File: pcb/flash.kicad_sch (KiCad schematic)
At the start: 11 parts, among them U5 W25Q128JVS

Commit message: Add MPN field for components except resistors
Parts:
- C24: MPN (none) -> CL10B104KB8NNWC
- TP12, TP13, TP14, TP15, TP16, TP17: MPN (none) -> RCUCTE
- U5: MPN (none) -> W25Q128JVS
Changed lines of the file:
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@@
+			)
+		)
+		(property "MPN" "RCUCTE"
+			(at 63.5 73.66 0)
+			(effects
+				(font
+					(size 1.27 1.27)
+				)
+				(hide yes)
 			)
 		)
@@
 			)
 		)
+		(property "MPN" "RCUCTE"
+			(at 63.5 63.5 0)
+			(effects
+				(font
+					(size 1.27 1.27)
+				)
+				(hide yes)
+			)
+		)
 		(pin "1"
 		)
@@
 			)
 		)
+		(property "MPN" ""
+			(at 76.2 50.8 0)
+			(effects
+				(font
+					(size 1.27 1.27)
+				)
+				(hide yes)
+			)
+		)
 		(pin "2"
 		)
@@
 		)
 		(property "Description" "Resistor, small US symbol"
+			(at 88.9 50.8 0)
+			(effects
+				(font
+					(size 1.27 1.27)
+				)
+				(hide yes)
+			)
+		)
+		(property "MPN" ""
 			(at 88.9 50.8 0)
 			(effects
@@
 			)
 		)
+		(property "MPN" "W25Q128JVS"
+			(at 101.6 76.2 0)
+			(effects
+				(font
+					(size 1.27 1.27)
+				)
+				(hide yes)
+			)
+		)
 		(pin "8"
 		)
@@
 			)
 		)
+		(property "MPN" "RCUCTE"
+			(at 63.5 83.82 0)
+			(effects
+				(font
+					(size 1.27 1.27)
+				)
+				(hide yes)
+			)
+		)
 		(pin "1"
 		)
@@
 			)
 		)
+		(property "MPN" "RCUCTE"
+			(at 63.5 88.9 0)
+			(effects
+				(font
+					(size 1.27 1.27)
+				)
+				(hide yes)
+			)
+		)
 		(pin "1"
 		)
@@
 		)
 		(property "Description" "Resistor, small US symbol"
+			(at 82.55 50.8 0)
+			(effects
+				(font
+					(size 1.27 1.27)
+				)
+				(hide yes)
+			)
+		)
+		(property "MPN" ""
 			(at 82.55 50.8 0)
 			(effects
@@
 			)
 		)
+		(property "MPN" "CL10B104KB8NNWC"
+			(at 114.3 50.8 0)
+			(effects
+				(font
+					(size 1.27 1.27)
+				)
+				(hide yes)
+			)
+		)
 		(pin "1"
 		)
@@
 			)
 		)
+		(property "MPN" "RCUCTE"
+			(at 63.5 78.74 0)
+			(effects
+				(font
+					(size 1.27 1.27)
+				)
+				(hide yes)
+			)
+		)
 		(pin "1"
 		)
@@
 			(at 63.5 68.58 0)
 			(effects
+				(font
+					(size 1.27 1.27)
+				)
+				(hide yes)
+			)
+		)
+		(property "MPN" "RCUCTE"
+			(at 63.5 68.58 0)
+			(effects

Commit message: Update resistor MPNs
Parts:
- R20, R21, R22: MPN (none) -> RC0603FR-0747KL
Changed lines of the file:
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@@
 			)
 		)
-		(property "MPN" ""
+		(property "MPN" "RC0603FR-0747KL"
 			(at 76.2 50.8 0)
 			(effects
@@
 			)
 		)
-		(property "MPN" ""
+		(property "MPN" "RC0603FR-0747KL"
 			(at 88.9 50.8 0)
 			(effects
@@
 			)
 		)
-		(property "MPN" ""
+		(property "MPN" "RC0603FR-0747KL"
 			(at 82.55 50.8 0)
 			(effects

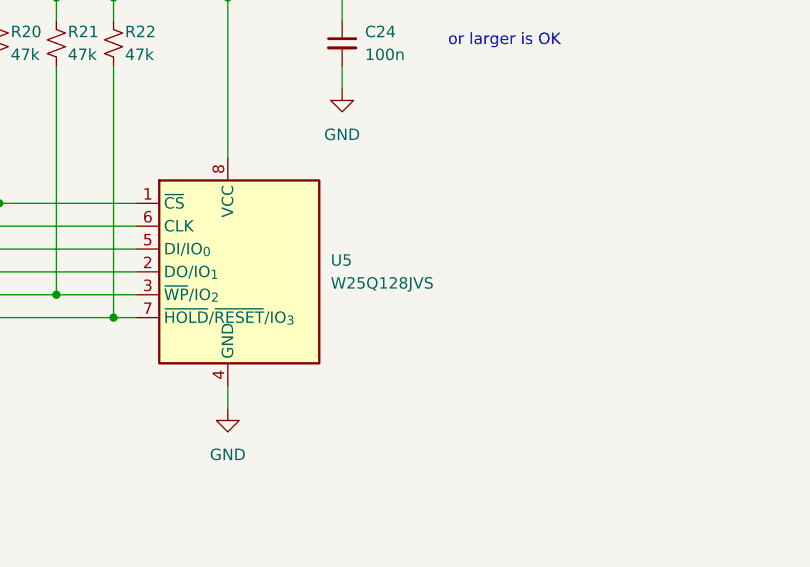
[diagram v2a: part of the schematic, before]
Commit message: Update MPNs to optimize for HQ Online
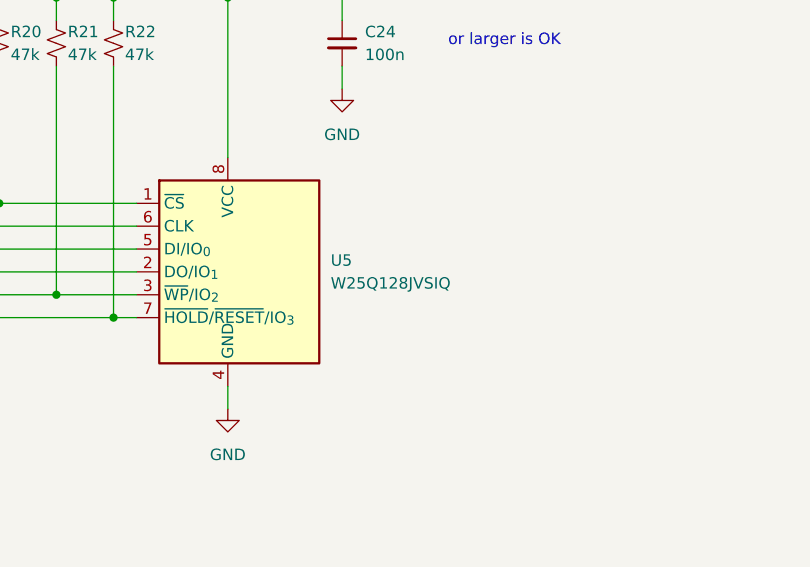
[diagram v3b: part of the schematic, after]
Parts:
- U5: value W25Q128JVS -> W25Q128JVSIQ; MPN W25Q128JVS -> W25Q128JVSIQ
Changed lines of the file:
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@@
 			)
 		)
-		(property "Value" "W25Q128JVS"
+		(property "Value" "W25Q128JVSIQ"
 			(at 113.03 77.4699 0)
 			(effects
@@
 			)
 		)
-		(property "MPN" "W25Q128JVS"
+		(property "MPN" "W25Q128JVSIQ"
 			(at 101.6 76.2 0)
 			(effects

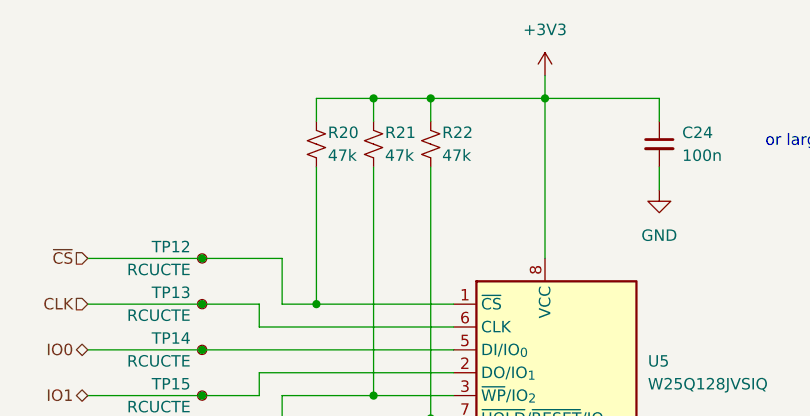
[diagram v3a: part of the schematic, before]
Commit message: Redo layout and routing for RGB LEDs
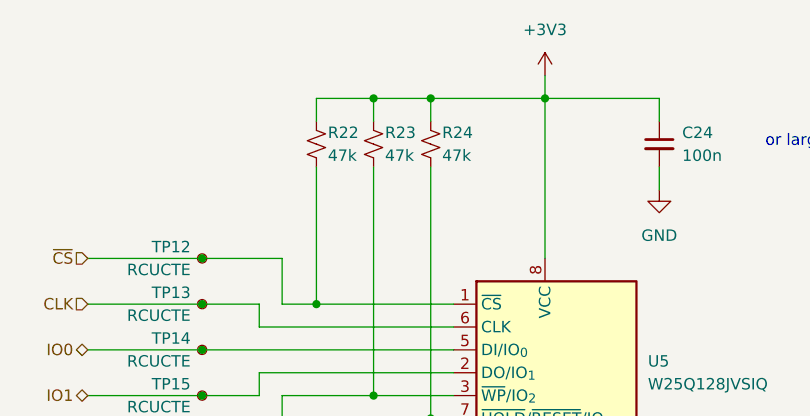
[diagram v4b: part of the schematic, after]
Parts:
- renumbered R20 to R22, R21 to R23, R22 to R24
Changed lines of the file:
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@@
 		(on_board yes)
 		(dnp no)
-		(property "Reference" "R20"
+		(property "Reference" "R22"
 			(at 77.47 49.53 0)
 			(effects
@@
 			(project "airbrake_mod"
 				(path "/1f4fd4ed-9886-4375-a5ac-dc32d5760936/676f83b0-0619-4d44-bbd6-46e3265a2238"
-					(reference "R20")
+					(reference "R22")
 					(unit 1)
 				)
@@
 		(on_board yes)
 		(dnp no)
-		(property "Reference" "R22"
+		(property "Reference" "R24"
 			(at 90.17 49.53 0)
 			(effects
@@
 			(project "airbrake_mod"
 				(path "/1f4fd4ed-9886-4375-a5ac-dc32d5760936/676f83b0-0619-4d44-bbd6-46e3265a2238"
-					(reference "R22")
+					(reference "R24")
 					(unit 1)
 				)
@@
 		(on_board yes)
 		(dnp no)
-		(property "Reference" "R21"
+		(property "Reference" "R23"
 			(at 83.82 49.53 0)
 			(effects
@@
 			(project "airbrake_mod"
 				(path "/1f4fd4ed-9886-4375-a5ac-dc32d5760936/676f83b0-0619-4d44-bbd6-46e3265a2238"
-					(reference "R21")
-					(unit 1)
-				)
+					(reference "R23")
+					(unit 1)
+				)
